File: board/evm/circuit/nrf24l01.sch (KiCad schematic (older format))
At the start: 1 part

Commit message: add lots of ICs
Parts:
- removed U?: STM32F405VGTx, LQFP100, symbol STM32F405VGTx
- added U?: nRF24L01, symbol nRF24L01
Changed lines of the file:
@@
 EELAYER 25 0
 EELAYER END
-$Descr A2 23386 16535
+$Descr A4 11693 8268
 encoding utf-8
-Sheet 2 8
+Sheet 5 8
 Title ""
 Date ""
@@
 $EndDescr
 $Comp
-L STM32F405VGTx U?
-U 1 1 5753F449
-P 9650 6400
-F 0 "U?" H 5350 9225 50  0000 L BNN
-F 1 "STM32F405VGTx" H 13950 9225 50  0000 R BNN
-F 2 "LQFP100" H 13950 9175 50  0000 R TNN
-F 3 "" H 9650 6400 50  0000 C CNN
-	1    9650 6400
+L nRF24L01 U?
+U 1 1 57546732
+P 3050 2250
+F 0 "U?" H 3050 2250 60  0000 C CNN
+F 1 "nRF24L01" H 3050 2400 60  0000 C CNN
+F 2 "" H 3450 1700 60  0000 C CNN
+F 3 "" H 3450 1700 60  0000 C CNN
+	1    3050 2250
 	1    0    0    -1
 $EndComp

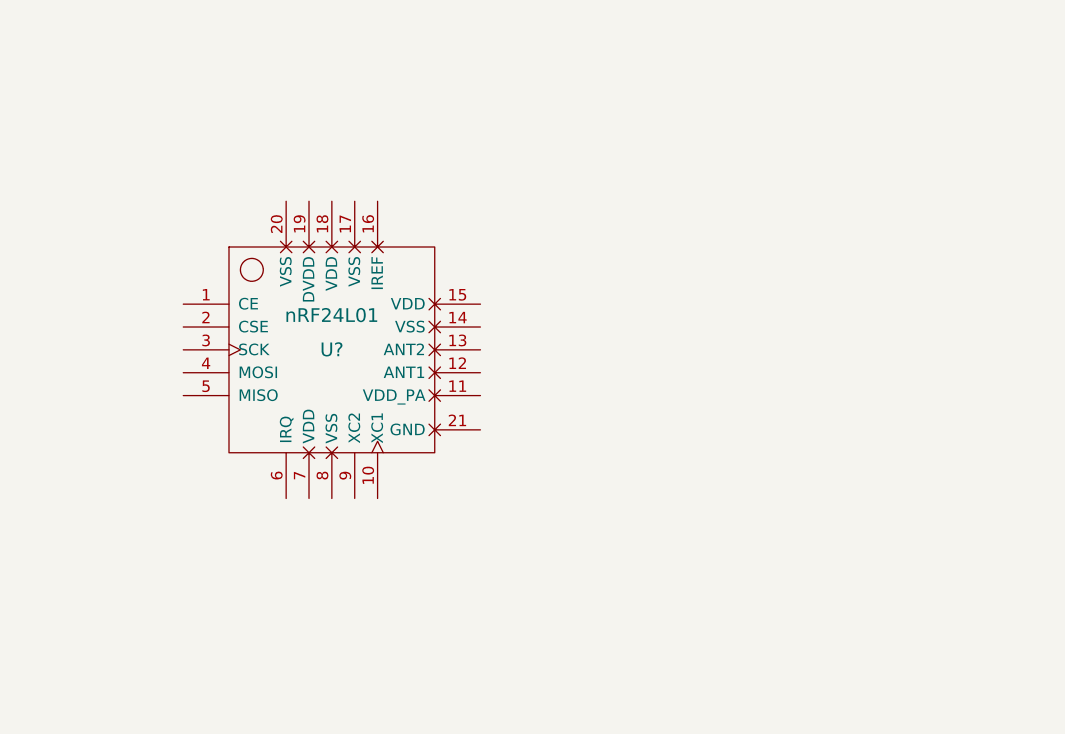
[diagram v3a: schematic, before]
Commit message: still working for sch
All done except for battery, which need more consideration on scheme of
QC2.0 (or QC3.0?), bidirectional charge.
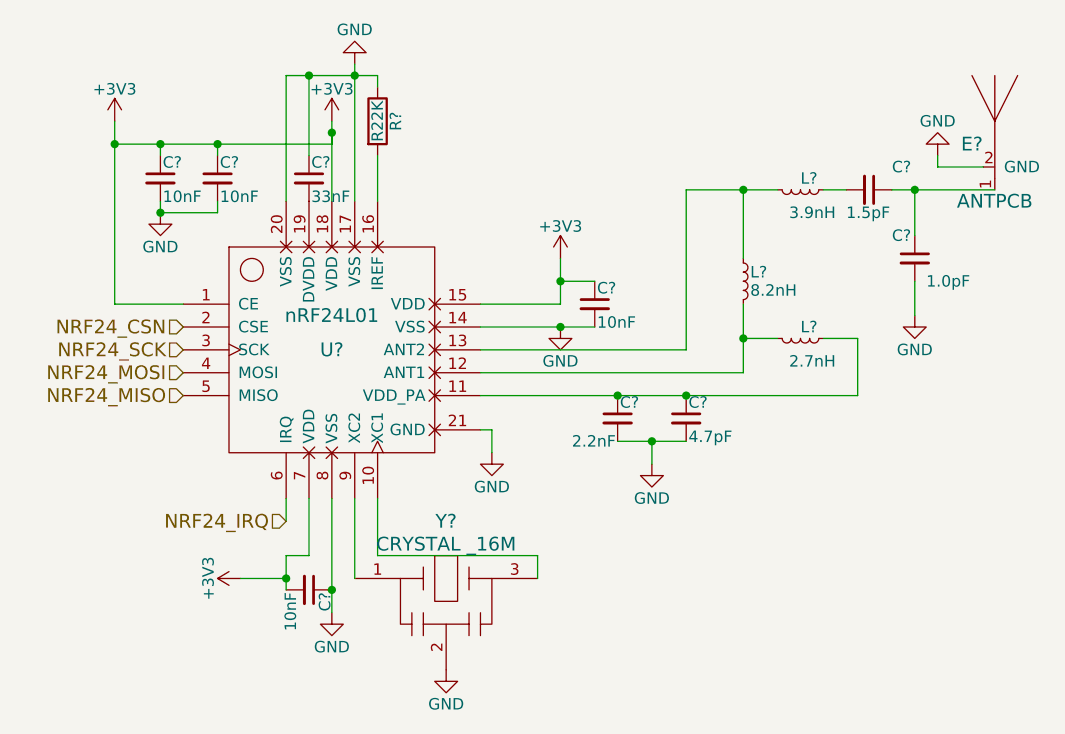
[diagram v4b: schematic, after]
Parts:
- added C?: 33nF, symbol C_Small
- added C? (x4): 10nF, symbol C_Small
- added C?: 2.2nF, symbol C_Small
- added C?: 4.7pF, symbol C_Small
- added C?: 1.0pF, symbol C_Small
- added C?: 1.5pF, symbol C_Small
- added E?: ANTPCB, symbol ANTPCB
- added L?: 8.2nH, symbol L_Small
- added L?: 2.7nH, symbol L_Small
- added L?: 3.9nH, symbol L_Small
- added R?: R22K, symbol R
- added Y?: CRYSTAL _16M, symbol CRYSTAL_SMT
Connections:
- net +3V3: now reaches U?.1 (CE)
- net +3V3: now also U?.15 (VDD), U?.18 (VDD), U?.7 (VDD), C?.1, C?.1, C?.1, C?.2
- net at U?.10 (XC1): now also Y?.3
- net at U?.11 (VDD_PA): now also C?.1, C?.1, L?.1
- net at U?.12 (ANT1): now also L?.2, L?.2
- net at U?.13 (ANT2): now also L?.1, L?.2
- net GND: now reaches U?.14 (VSS)
- net GND: now also U?.17 (VSS), U?.20 (VSS), U?.21 (GND), U?.8 (VSS), C?.1, C?.1, C?.2, C?.2, C?.2, C?.2, C?.2, C?.2, E?.2 (GND), R?.1, Y?.2
- net at U?.16 (IREF): now also R?.2
- net at U?.19 (DVDD): now also C?.2
- net NRF24_CSN: now reaches U?.2 (CSE)
- net NRF24_SCK: now reaches U?.3 (SCK)
- net NRF24_MOSI: now reaches U?.4 (MOSI)
- net NRF24_MISO: now reaches U?.5 (MISO)
- net NRF24_IRQ: now reaches U?.6 (IRQ)
- net at U?.9 (XC2): now also Y?.1
- new net: C?.2, L?.1
- new net: C?.1, C?.1, E?.1

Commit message: working on drc
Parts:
- gave numbers to parts that had none: 16
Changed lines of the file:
@@
 $EndDescr
 $Comp
-L nRF24L01 U?
+L nRF24L01 U7
 U 1 1 57546732
 P 3050 2250
-F 0 "U?" H 3050 2250 60  0000 C CNN
+F 0 "U7" H 3050 2250 60  0000 C CNN
 F 1 "nRF24L01" H 3050 2400 60  0000 C CNN
 F 2 "" H 3450 1700 60  0000 C CNN
@@
 NRF24_CSN
 $Comp
-L +3V3 #PWR?
+L +3V3 #PWR055
 U 1 1 575832CF
 P 2100 1250
-F 0 "#PWR?" H 2100 1100 50  0001 C CNN
+F 0 "#PWR055" H 2100 1100 50  0001 C CNN
 F 1 "+3V3" H 2100 1390 50  0000 C CNN
 F 2 "" H 2100 1250 50  0000 C CNN
@@
 NRF24_MISO
 $Comp
-L +3V3 #PWR?
+L +3V3 #PWR056
 U 1 1 575832FA
 P 4050 1850
-F 0 "#PWR?" H 4050 1700 50  0001 C CNN
+F 0 "#PWR056" H 4050 1700 50  0001 C CNN
 F 1 "+3V3" H 4050 1990 50  0000 C CNN
 F 2 "" H 4050 1850 50  0000 C CNN
@@
 $EndComp
 $Comp
-L +3V3 #PWR?
+L +3V3 #PWR057
 U 1 1 5758330E
 P 2650 3250
-F 0 "#PWR?" H 2650 3100 50  0001 C CNN
+F 0 "#PWR057" H 2650 3100 50  0001 C CNN
 F 1 "+3V3" H 2650 3390 50  0000 C CNN
 F 2 "" H 2650 3250 50  0000 C CNN
@@
 $EndComp
 $Comp
-L GND #PWR?
+L GND #PWR058
 U 1 1 57583325
 P 3050 3400
-F 0 "#PWR?" H 3050 3150 50  0001 C CNN
+F 0 "#PWR058" H 3050 3150 50  0001 C CNN
 F 1 "GND" H 3050 3250 50  0000 C CNN
 F 2 "" H 3050 3400 50  0000 C CNN
@@
 $EndComp
 $Comp
-L GND #PWR?
+L GND #PWR059
 U 1 1 57583344
 P 4050 2150
-F 0 "#PWR?" H 4050 1900 50  0001 C CNN
+F 0 "#PWR059" H 4050 1900 50  0001 C CNN
 F 1 "GND" H 4050 2000 50  0000 C CNN
 F 2 "" H 4050 2150 50  0000 C CNN
@@
 $EndComp
 $Comp
-L GND #PWR?
+L GND #PWR060
 U 1 1 5758335D
 P 3150 1000
-F 0 "#PWR?" H 3150 750 50  0001 C CNN
+F 0 "#PWR060" H 3150 750 50  0001 C CNN
 F 1 "GND" H 3150 850 50  0000 C CNN
 F 2 "" H 3150 1000 50  0000 C CNN
@@
 $EndComp
 $Comp
-L R R?
+L R R6
 U 1 1 57583379
 P 3250 1250
-F 0 "R?" V 3330 1250 50  0000 C CNN
+F 0 "R6" V 3330 1250 50  0000 C CNN
 F 1 "R22K" V 3250 1250 50  0000 C CNN
 F 2 "" V 3180 1250 50  0000 C CNN
@@
 $EndComp
 $Comp
-L +3V3 #PWR?
+L +3V3 #PWR061
 U 1 1 575833C0
 P 3050 1250
-F 0 "#PWR?" H 3050 1100 50  0001 C CNN
+F 0 "#PWR061" H 3050 1100 50  0001 C CNN
 F 1 "+3V3" H 3050 1390 50  0000 C CNN
 F 2 "" H 3050 1250 50  0000 C CNN
@@
 $EndComp
 $Comp
-L C_Small C?
+L C_Small C16
 U 1 1 575833E7
 P 2950 1500
-F 0 "C?" H 2960 1570 50  0000 L CNN
+F 0 "C16" H 2960 1570 50  0000 L CNN
 F 1 "33nF" H 2960 1420 50  0000 L CNN
 F 2 "" H 2950 1500 50  0000 C CNN
@@
 $EndComp
 $Comp
-L C_Small C?
+L C_Small C17
 U 1 1 575834D6
 P 2950 3300
-F 0 "C?" H 2960 3370 50  0000 L CNN
+F 0 "C17" H 2960 3370 50  0000 L CNN
 F 1 "10nF" H 2960 3220 50  0000 L CNN
 F 2 "" H 2950 3300 50  0000 C CNN
@@
 $EndComp
 $Comp
-L C_Small C?
+L C_Small C18
 U 1 1 5758357C
 P 4200 2050
-F 0 "C?" H 4210 2120 50  0000 L CNN
+F 0 "C18" H 4210 2120 50  0000 L CNN
 F 1 "10nF" H 4210 1970 50  0000 L CNN
 F 2 "" H 4200 2050 50  0000 C CNN
@@
 $EndComp
 $Comp
-L C_Small C?
+L C_Small C15
 U 1 1 57583604
 P 2550 1500
-F 0 "C?" H 2560 1570 50  0000 L CNN
+F 0 "C15" H 2560 1570 50  0000 L CNN
 F 1 "10nF" H 2560 1420 50  0000 L CNN
 F 2 "" H 2550 1500 50  0000 C CNN
@@
 $EndComp
 $Comp
-L C_Small C?
+L C_Small C14
 U 1 1 5758366E
 P 2300 1500
-F 0 "C?" H 2310 1570 50  0000 L CNN
+F 0 "C14" H 2310 1570 50  0000 L CNN
 F 1 "10nF" H 2310 1420 50  0000 L CNN
 F 2 "" H 2300 1500 50  0000 C CNN
@@
 $EndComp
 Wire Wire Line
-	2100 1250 2100 1350
-Wire Wire Line
-	2100 1350 2100 2050
+	2100 1250 2100 2050
 Wire Wire Line
 	2100 2050 2400 2050
@@
 	4050 2050 3700 2050
 Wire Wire Line
-	4050 1850 4050 1950
-Wire Wire Line
-	4050 1950 4050 2050
-Wire Wire Line
-	2850 3150 2850 3250
-Wire Wire Line
-	2850 3250 2850 3300
+	4050 1850 4050 2050
+Wire Wire Line
+	2850 3150 2850 3300
 Wire Wire Line
 	2850 3150 2950 3150
 Wire Wire Line
-	3050 2900 3050 3300
-Wire Wire Line
-	3050 3300 3050 3400
-Wire Wire Line
-	3700 2150 4050 2150
-Wire Wire Line
-	4050 2150 4200 2150
-Wire Wire Line
-	3150 1000 3150 1050
-Wire Wire Line
-	3150 1050 3150 1600
-Wire Wire Line
-	2850 1050 2950 1050
-Wire Wire Line
-	2950 1050 3150 1050
-Wire Wire Line
-	3150 1050 3250 1050
+	3050 2900 3050 3400
+Wire Wire Line
+	3700 2150 4200 2150
+Wire Wire Line
+	3150 1000 3150 1600
+Wire Wire Line
+	2850 1050 3250 1050
 Wire Wire Line
 	3250 1050 3250 1100
@@
 	3250 1400 3250 1600
 Wire Wire Line
-	3050 1250 3050 1300
-Wire Wire Line
-	3050 1300 3050 1600
+	3050 1250 3050 1600
 Wire Wire Line
 	2950 1400 2950 1050
@@
 Connection ~ 4050 1950
 Wire Wire Line
-	2100 1350 2300 1350
-Wire Wire Line
-	2300 1350 2550 1350
-Wire Wire Line
-	2550 1350 3050 1350
+	2100 1350 3050 1350
 Connection ~ 2100 1350
 Wire Wire Line
@@
 	2550 1650 2550 1600
 $Comp
-L GND #PWR?
+L GND #PWR062
 U 1 1 575837FB
 P 2300 1650
-F 0 "#PWR?" H 2300 1400 50  0001 C CNN
+F 0 "#PWR062" H 2300 1400 50  0001 C CNN
 F 1 "GND" H 2300 1500 50  0000 C CNN
 F 2 "" H 2300 1650 50  0000 C CNN
@@
 Connection ~ 2300 1650
 $Comp
-L GND #PWR?
+L GND #PWR063
 U 1 1 57583B29
 P 3750 2700
-F 0 "#PWR?" H 3750 2450 50  0001 C CNN
+F 0 "#PWR063" H 3750 2450 50  0001 C CNN
 F 1 "GND" H 3750 2550 50  0000 C CNN
 F 2 "" H 3750 2700 50  0000 C CNN
@@
 	3750 2600 3750 2700
 $Comp
-L CRYSTAL_SMT Y?
+L CRYSTAL_SMT Y1
 U 1 1 57583C37
 P 3550 3300
-F 0 "Y?" H 3550 3600 60  0000 C CNN
+F 0 "Y1" H 3550 3600 60  0000 C CNN
 F 1 "CRYSTAL_16M" H 3550 3500 60  0000 C CNN
 F 2 "" H 3550 3300 60  0000 C CNN
@@
 	3950 3150 3950 3250
 $Comp
-L GND #PWR?
+L GND #PWR064
 U 1 1 57583CE0
 P 3550 3650
-F 0 "#PWR?" H 3550 3400 50  0001 C CNN
+F 0 "#PWR064" H 3550 3400 50  0001 C CNN
 F 1 "GND" H 3550 3500 50  0000 C CNN
 F 2 "" H 3550 3650 50  0000 C CNN
@@
 Connection ~ 2850 3250
 $Comp
-L C_Small C?
+L C_Small C19
 U 1 1 57584348
 P 4300 2550
-F 0 "C?" H 4310 2620 50  0000 L CNN
+F 0 "C19" H 4310 2620 50  0000 L CNN
 F 1 "2.2nF" H 4100 2450 50  0000 L CNN
 F 2 "" H 4300 2550 50  0000 C CNN
@@
 $EndComp
 $Comp
-L C_Small C?
+L C_Small C20
 U 1 1 575843A6
 P 4600 2550
-F 0 "C?" H 4610 2620 50  0000 L CNN
+F 0 "C20" H 4610 2620 50  0000 L CNN
 F 1 "4.7pF" H 4610 2470 50  0000 L CNN
 F 2 "" H 4600 2550 50  0000 C CNN
@@
 	4600 2250 4600 1550
 Wire Wire Line
-	4600 1550 4850 1550
-Wire Wire Line
-	4850 1550 5000 1550
+	4600 1550 5000 1550
 Wire Wire Line
 	4850 2350 3700 2350
 Wire Wire Line
-	4850 2050 4850 2200
-Wire Wire Line
-	4850 2200 4850 2350
-$Comp
-L L_Small L?
+	4850 2050 4850 2350
+$Comp
+L L_Small L1
 U 1 1 575844A4
 P 4850 1950
-F 0 "L?" H 4880 1990 50  0000 L CNN
+F 0 "L1" H 4880 1990 50  0000 L CNN
 F 1 "8.2nH" H 4880 1910 50  0000 L CNN
 F 2 "" H 4850 1950 50  0000 C CNN
@@
 $EndComp
 $Comp
-L L_Small L?
+L L_Small L3
 U 1 1 57584559
 P 5100 2200
-F 0 "L?" V 5050 2200 50  0000 L CNN
+F 0 "L3" V 5050 2200 50  0000 L CNN
 F 1 "2.7nH" V 5200 2150 50  0000 L CNN
 F 2 "" H 5100 2200 50  0000 C CNN
@@
 Connection ~ 4850 1550
 $Comp
-L L_Small L?
+L L_Small L2
 U 1 1 57584771
 P 5100 1550
-F 0 "L?" V 5050 1550 50  0000 L CNN
+F 0 "L2" V 5050 1550 50  0000 L CNN
 F 1 "3.9nH" V 5200 1500 50  0000 L CNN
 F 2 "" H 5100 1550 50  0000 C CNN
@@
 $EndComp
 $Comp
-L C_Small C?
+L C_Small C22
 U 1 1 57584807
 P 5600 1850
-F 0 "C?" H 5500 1950 50  0000 L CNN
+F 0 "C22" H 5500 1950 50  0000 L CNN
 F 1 "1.0pF" H 5650 1750 50  0000 L CNN
 F 2 "" H 5600 1850 50  0000 C CNN
@@
 $EndComp
 $Comp
-L C_Small C?
+L C_Small C21
 U 1 1 57584B39
 P 5400 1550
-F 0 "C?" V 5300 1650 50  0000 L CNN
+F 0 "C21" V 5300 1650 50  0000 L CNN
 F 1 "1.5pF" V 5500 1450 50  0000 L CNN
 F 2 "" H 5400 1550 50  0000 C CNN
@@
 	5300 1550 5200 1550
 Wire Wire Line
-	5500 1550 5600 1550
-Wire Wire Line
-	5600 1550 5950 1550
+	5500 1550 5950 1550
 Wire Wire Line
 	5600 1550 5600 1750
 $Comp
-L GND #PWR?
+L GND #PWR065
 U 1 1 57584D58
 P 5600 2100
-F 0 "#PWR?" H 5600 1850 50  0001 C CNN
+F 0 "#PWR065" H 5600 1850 50  0001 C CNN
 F 1 "GND" H 5600 1950 50  0000 C CNN
 F 2 "" H 5600 2100 50  0000 C CNN
@@
 	5200 2200 5350 2200
 Wire Wire Line
-	5350 2450 5350 2200
-Wire Wire Line
-	3700 2450 4300 2450
-Wire Wire Line
-	4300 2450 4600 2450
-Wire Wire Line
-	4600 2450 5350 2450
+	5350 2200 5350 2450
+Wire Wire Line
+	5350 2450 3700 2450
 Connection ~ 4600 2450
 Connection ~ 4300 2450
 Wire Wire Line
-	4300 2650 4450 2650
-Wire Wire Line
-	4450 2650 4600 2650
-$Comp
-L GND #PWR?
+	4300 2650 4600 2650
+$Comp
+L GND #PWR066
 U 1 1 57584F30
 P 4450 2750
-F 0 "#PWR?" H 4450 2500 50  0001 C CNN
+F 0 "#PWR066" H 4450 2500 50  0001 C CNN
 F 1 "GND" H 4450 2600 50  0000 C CNN
 F 2 "" H 4450 2750 50  0000 C CNN
@@
 Connection ~ 4450 2650
 $Comp
-L ANTPCB E?
+L ANTPCB E1
 U 1 1 575850E1
 P 5950 1500
-F 0 "E?" H 5850 1650 60  0000 C CNN
+F 0 "E1" H 5850 1650 60  0000 C CNN
 F 1 "ANTPCB" H 5950 1400 60  0000 C CNN
 F 2 "" H 5950 1500 60  0000 C CNN
@@
 	5700 1450 5700 1400
 $Comp
-L GND #PWR?
+L GND #PWR067
 U 1 1 57585646
 P 5700 1400
-F 0 "#PWR?" H 5700 1150 50  0001 C CNN
+F 0 "#PWR067" H 5700 1150 50  0001 C CNN
 F 1 "GND" H 5700 1250 50  0000 C CNN
 F 2 "" H 5700 1400 50  0000 C CNN
